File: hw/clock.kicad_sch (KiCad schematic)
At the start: 3 parts, among them SW1 SW_Push, U1 ATMEGA328PB-AU

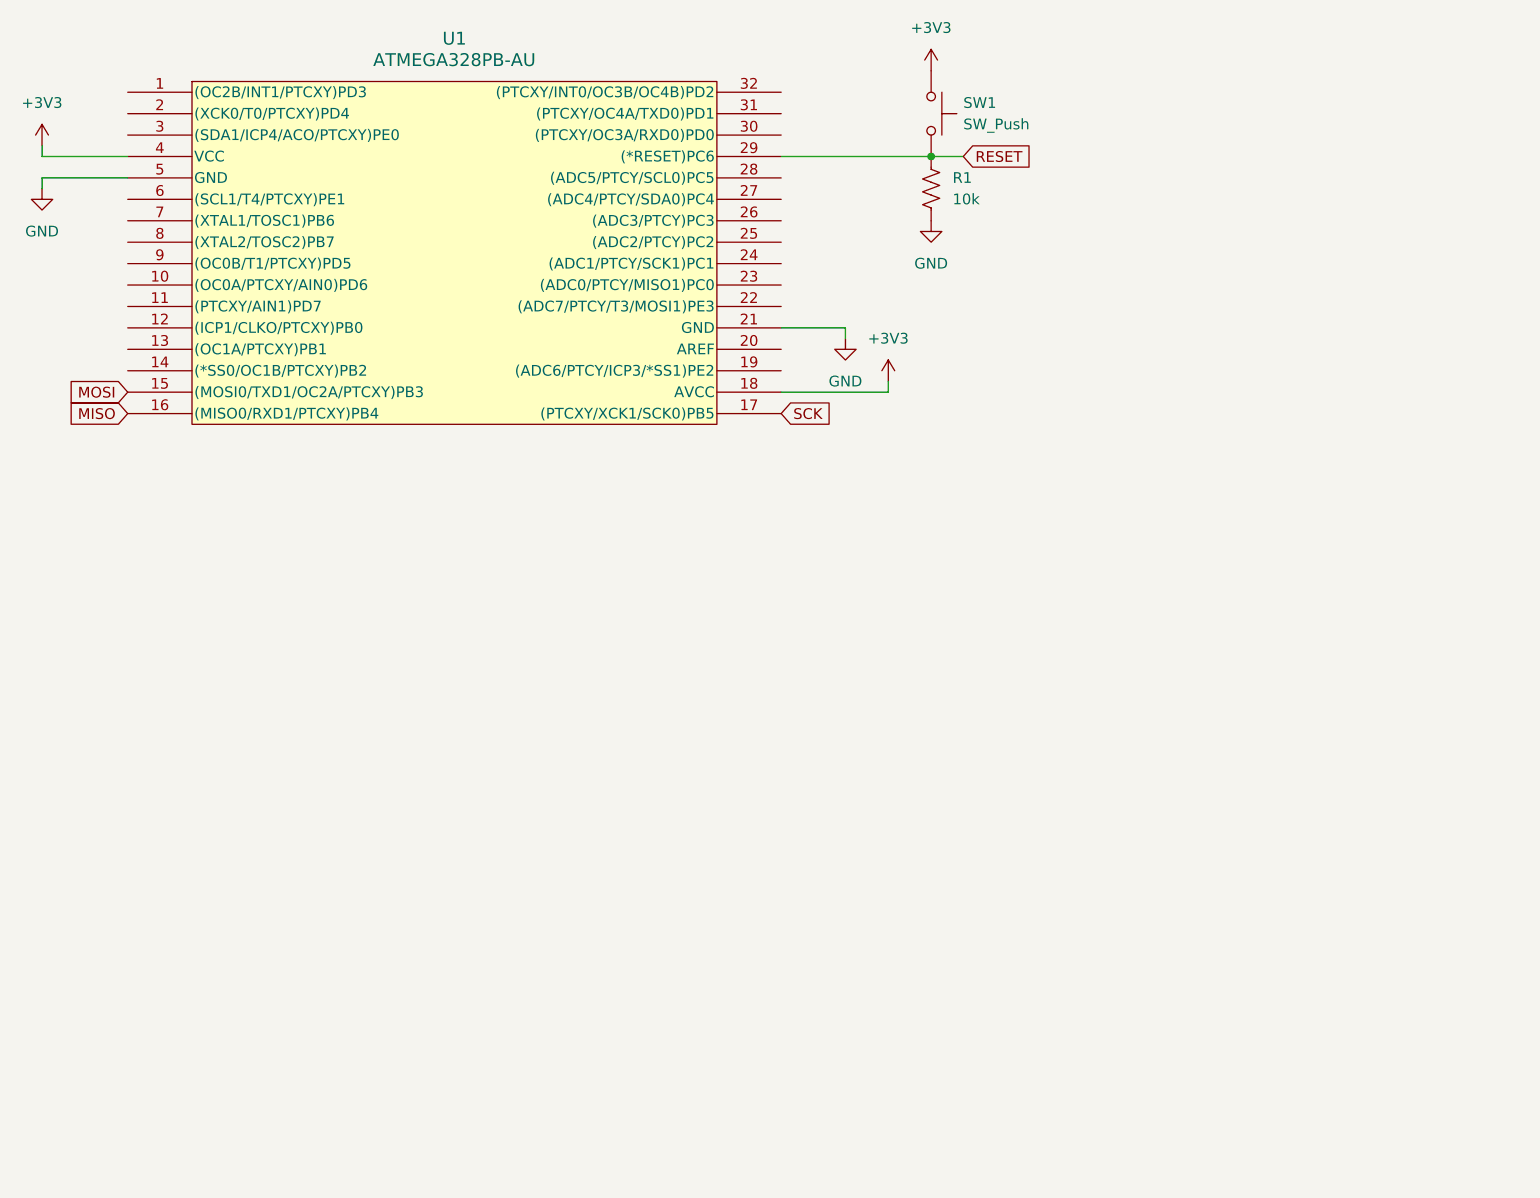
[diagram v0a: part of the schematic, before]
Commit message: Add USB
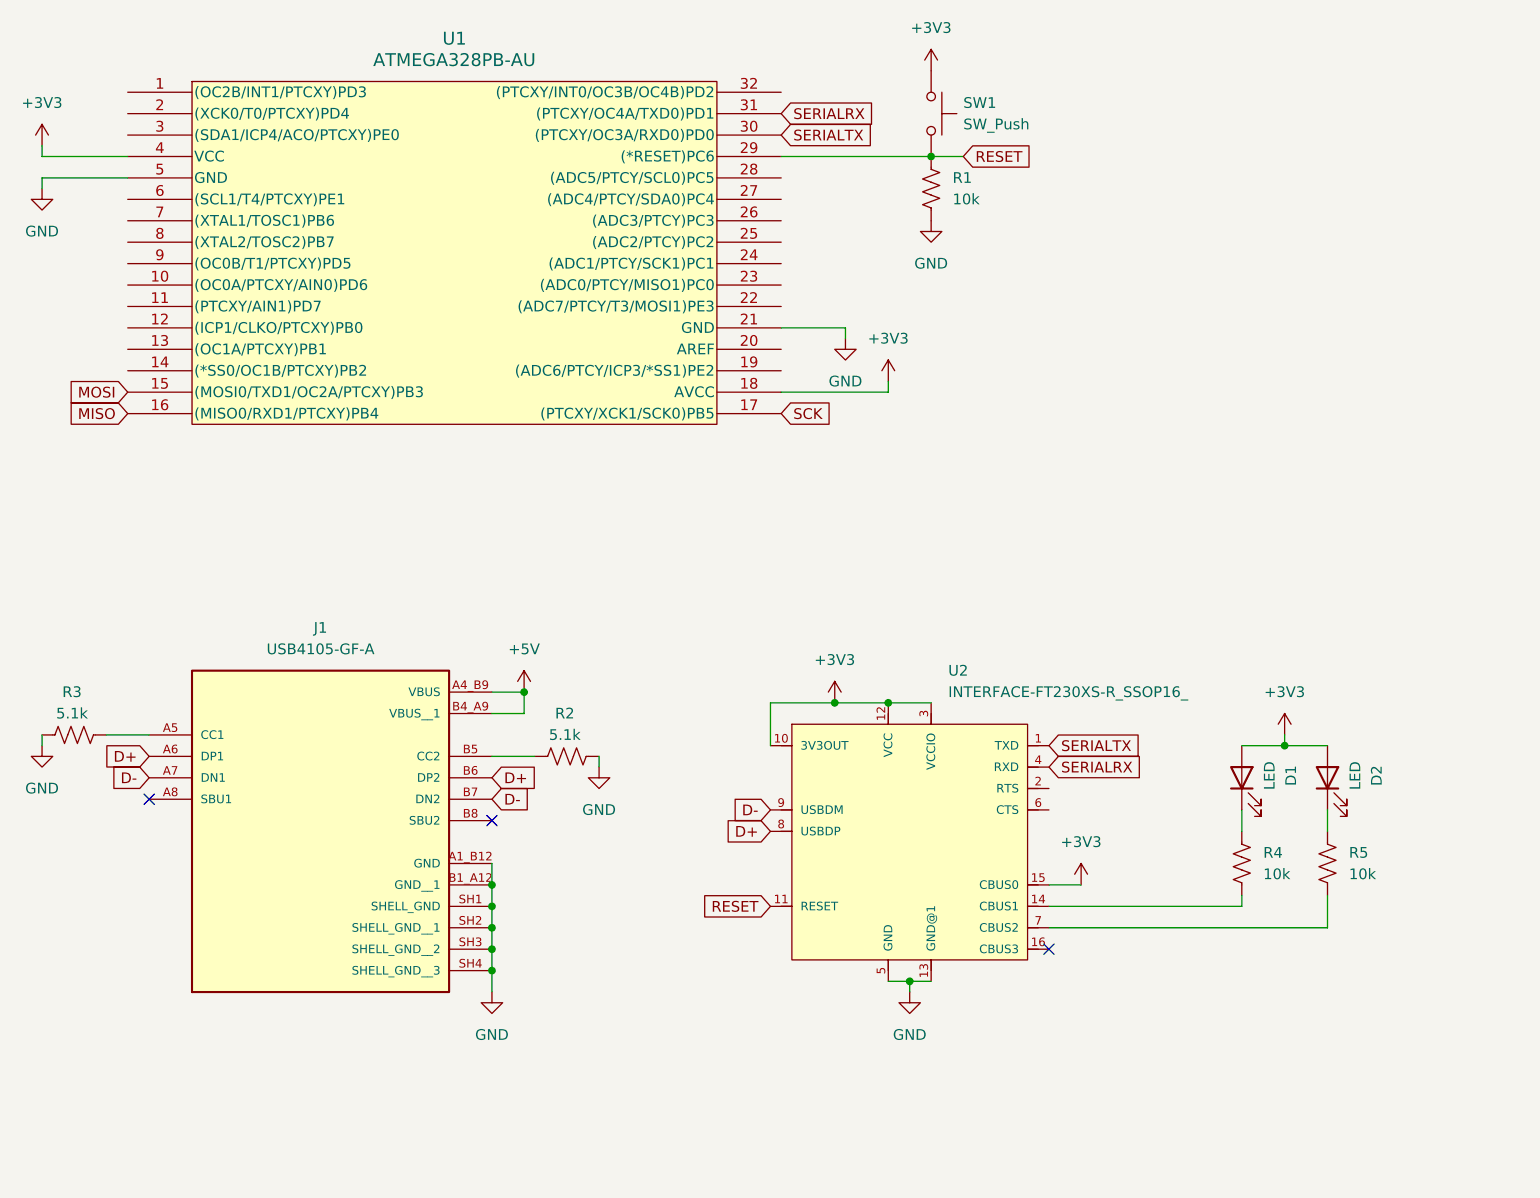
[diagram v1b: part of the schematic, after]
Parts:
- added D1, D2: LED, symbol Device:LED
- added J1: USB4105-GF-A, USB4105-GF-A:GCT_USB4105-GF-A, symbol USB4105-GF-A:USB4105-GF-A
- added R2, R3: 5.1k, symbol Device:R_US
- added R4, R5: 10k, symbol Device:R_US
- added U2: INTERFACE-FT230XS-R_SSOP16_, INTERFACE-FT230XS-R_SSOP16_:SSOP16-0.635-5X4MM, symbol INTERFACE-FT230XS-R_SSOP16_:INTERFACE-FT230XS-R_SSOP16_
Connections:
- net +3V3: now also D1.2 (A), D2.2 (A), U2.10 (3V3OUT), U2.12 (VCC), U2.15 (CBUS0), U2.3 (VCCIO)
- net GND: now also J1.A1_B12 (GND), J1.B1_A12 (GND__1), J1.SH1 (SHELL_GND), J1.SH2 (SHELL_GND__1), J1.SH3 (SHELL_GND__2), J1.SH4 (SHELL_GND__3), R2.1, R3.2, U2.13 (GND@1), U2.5 (GND)
- net RESET: now also U2.11 (RESET)
- net SERIALTX: now reaches U1.30 ((PTCXY/OC3A/RXD0)PD0)
- net SERIALTX: now also U2.1 (TXD)
- net SERIALRX: now reaches U1.31 ((PTCXY/OC4A/TXD0)PD1)
- net SERIALRX: now also U2.4 (RXD)
- new net: D1.1 (K), R4.2
- new net: D2.1 (K), R5.2
- new net: R4.1, U2.14 (CBUS1)
- new net: R5.1, U2.7 (CBUS2)
- new net: J1.A5 (CC1), R3.1
- new net: J1.B5 (CC2), R2.2
- new net +5V: J1.A4_B9 (VBUS), J1.B4_A9 (VBUS__1)
- new net D+: J1.A6 (DP1), J1.B6 (DP2), U2.8 (USBDP)
- new net D-: J1.A7 (DN1), J1.B7 (DN2), U2.9 (USBDM)
- no-connect marks 0 -> 3

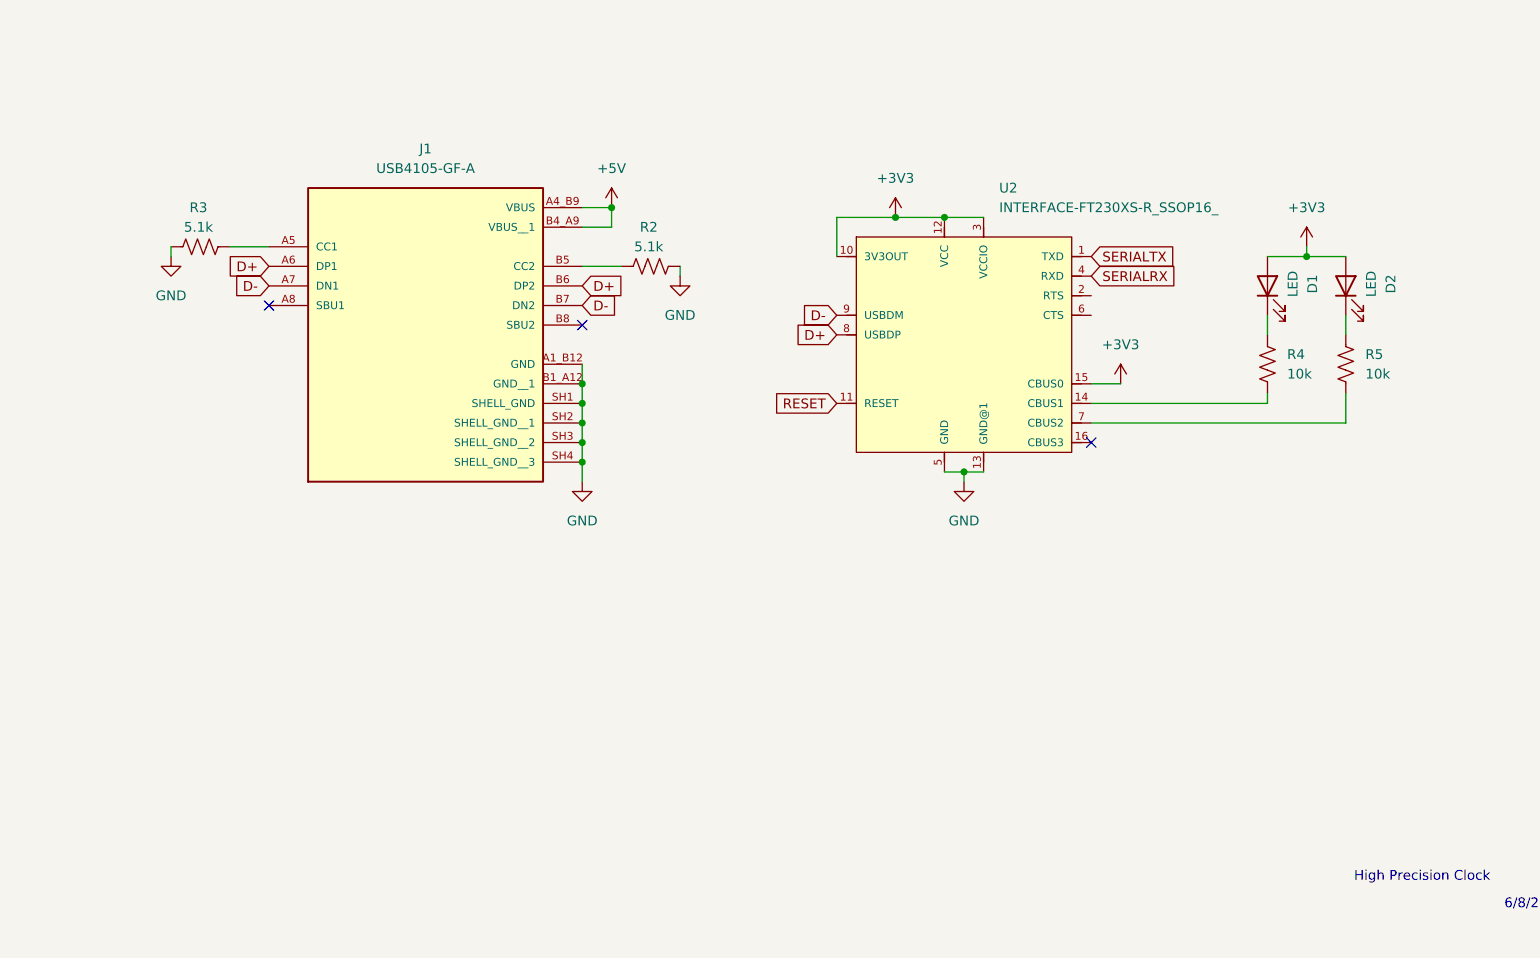
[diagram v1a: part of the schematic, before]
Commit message: Add voltage reg and serial converter
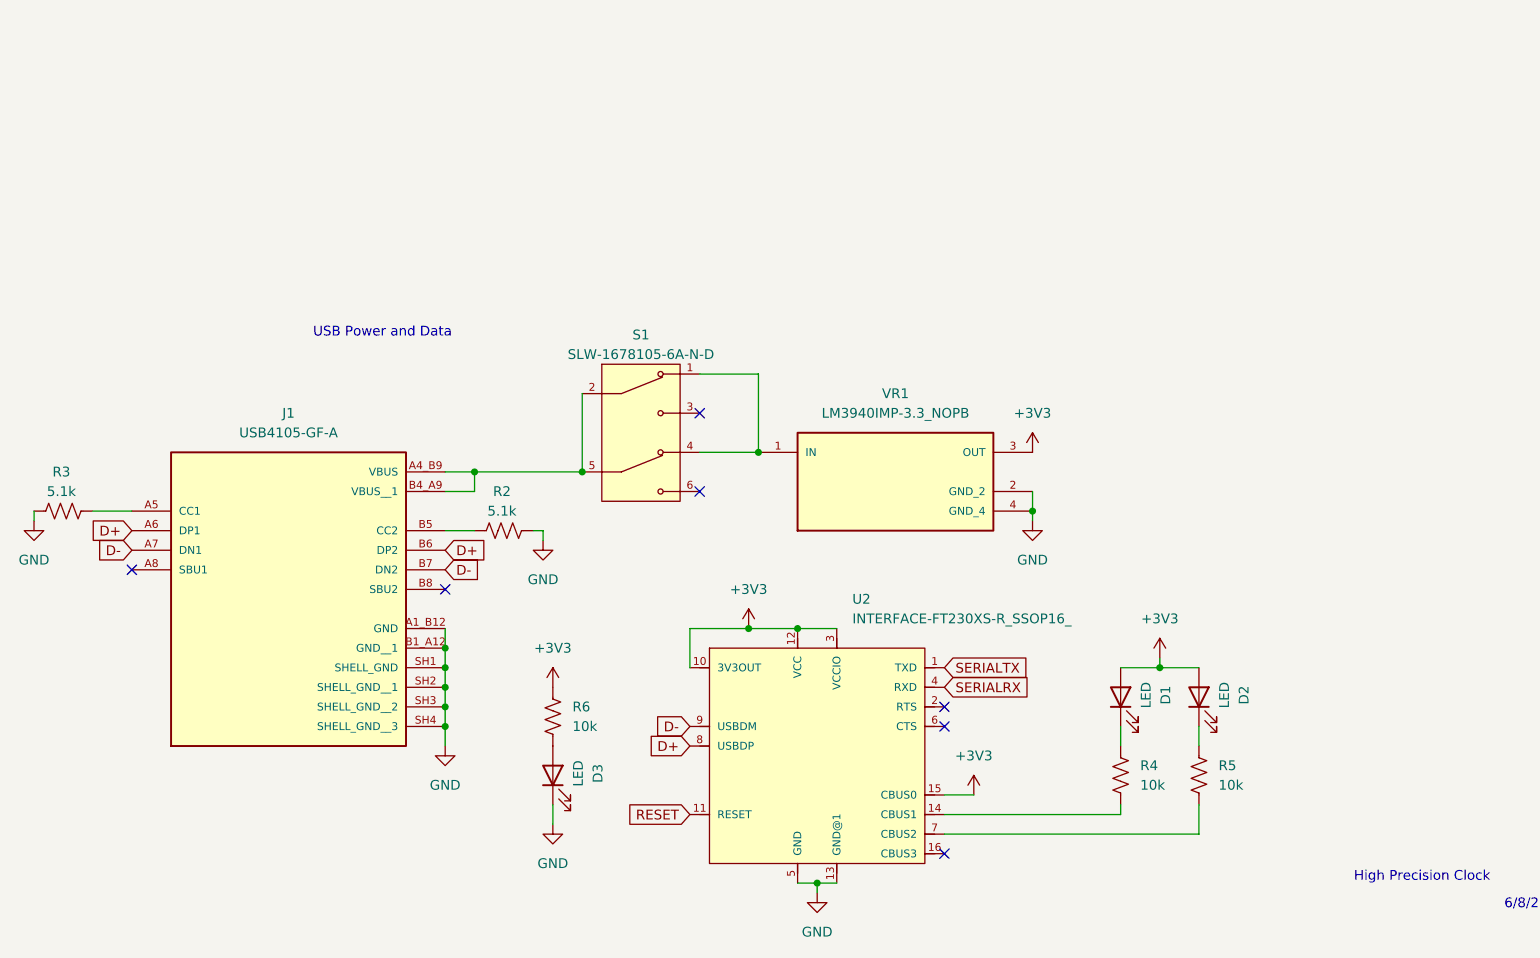
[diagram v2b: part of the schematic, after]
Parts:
- added D3: LED, LED_SMD:LED_0805_2012Metric, symbol Device:LED
- added R6: 10k, Resistor_SMD:R_0805_2012Metric, symbol Device:R_US
- added S1: SLW-1678105-6A-N-D, Clock:SW_SLW-1678105-6A-N-D, symbol SLW-1678105-6A-N-D:SLW-1678105-6A-N-D
- added VR1: LM3940IMP-3.3_NOPB, Clock:VREG_LM3940IMP-3.3_NOPB, symbol LM3940IMP-3.3_NOPB:LM3940IMP-3.3_NOPB
- D1, D2: footprint (none) -> LED_SMD:LED_0805_2012Metric
- J1: footprint USB4105-GF-A:GCT_USB4105-GF-A -> Clock:GCT_USB4105-GF-A
- R1, R2, R3, R4, R5: footprint (none) -> Resistor_SMD:R_0805_2012Metric
- U1: footprint 32A_MCH -> Clock:32A_MCH
- U2: footprint INTERFACE-FT230XS-R_SSOP16_:SSOP16-0.635-5X4MM -> Clock:SSOP16-0.635-5X4MM
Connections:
- net +3V3: now also R6.2, VR1.3 (OUT)
- net GND: now also D3.1 (K), VR1.2 (GND_2), VR1.4 (GND_4)
- net +5V: no longer names the net of J1.A4_B9 (VBUS), J1.B4_A9 (VBUS__1)
- net +5V: now also S1.2, S1.5
- new net: S1.1, S1.4, VR1.1 (IN)
- new net: D3.2 (A), R6.1
- no-connect marks 3 -> 7
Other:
- note added: "USB Power and Data"
- moved on the sheet: D1, D2, J1, R2, R3, R4, R5, U2

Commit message: Change mcu
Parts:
- removed R1: 10k, Resistor_SMD:R_0805_2012Metric, symbol Device:R_US
- removed SW1: SW_Push, symbol Switch:SW_Push
- removed U1: ATMEGA328PB-AU, Clock:32A_MCH, symbol 32A_MCH:ATMEGA328PB-AU
- added C1, C2: 20pf, symbol Device:C
- added R7: 10k, Resistor_SMD:R_0805_2012Metric, symbol Device:R_US
- added SW2: SW_Push, symbol Switch:SW_Push
- added U1: LPC812M101JDH20, Package_SO:TSSOP-20_4.4x6.5mm_P0.65mm, symbol MCU_NXP_LPC:LPC812M101JDH20
- added Y1: 30MHz, symbol Device:Crystal
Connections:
- net +3V3: now also SW2.1, U1.15 (VDD)
- net GND: now also C1.2, C2.1, R7.1, U1.16 (VSS)
- net RESET: now also R7.2, SW2.2, U1.4 (PIO0_5)
- net +5V: now reaches J1.A4_B9 (VBUS), J1.B4_A9 (VBUS__1), S1.2, S1.5
- net SERIALRX renamed SERIAL2
- net SERIAL2: now also U1.5 (PIO0_4)
- net SERIALTX renamed SERIAL1
- net SERIAL1: now also U1.19 (PIO0_0)
- new net: C1.1, U1.14 (PIO0_8), Y1.1
- new net: C2.2, U1.13 (PIO0_9), Y1.2
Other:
- note added: "RX"
- note added: "Serial lines used for audio data and programming"
- note added: "TX"

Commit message: Shift registers
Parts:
- removed SW2: SW_Push, symbol Switch:SW_Push
- added SW1: SW_Push, symbol Switch:SW_Push
- added U3, U4, U5, U6, U7, U8: SN74HC595DR, SN74HC595DR:SOIC127P600X175-16N, symbol SN74HC595DR:SN74HC595DR
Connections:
- net +3V3: now also U2.11 (RESET), SW1.1, U3.16 (VCC), U4.16 (VCC), U5.16 (VCC), U6.16 (VCC), U7.16 (VCC), U8.16 (VCC)
- net GND: now also U3.8 (GND), U4.8 (GND), U5.8 (GND), U6.8 (GND), U7.8 (GND), U8.8 (GND)
- net SHIFT_SER_0: now reaches U1.17 (PIO0_7)
- net SHIFT_SER_0: now also U3.14 (SER)
- net SHIFT_CLK: now reaches U1.18 (PIO0_6)
- net SHIFT_CLK: now also U3.11 (SRCLK), U4.11 (SRCLK), U5.11 (SRCLK), U6.11 (SRCLK), U7.11 (SRCLK), U8.11 (SRCLK)
- net SHIFT_SER_4: now reaches U1.2 (PIO0_13)
- net SHIFT_SER_4: now also U7.14 (SER)
- net SHIFT_SER_5: now reaches U1.20 (PIO0_14)
- net SHIFT_SER_5: now also U8.14 (SER)
- net SHIFT_SER_3: now reaches U1.3 (PIO0_12)
- net SHIFT_SER_3: now also U6.14 (SER)
- net SHIFT_RCLK: now reaches U1.6 (PIO0_3)
- net SHIFT_RCLK: now also U3.12 (RCLK), U4.12 (RCLK), U5.12 (RCLK), U6.12 (RCLK), U7.12 (RCLK), U8.12 (RCLK)
- net SHIFT_CLR: now reaches U1.7 (PIO0_2)
- net SHIFT_CLR: now also U3.10 (~{SRCLR}), U4.10 (~{SRCLR}), U5.10 (~{SRCLR}), U6.10 (~{SRCLR}), U7.10 (~{SRCLR}), U8.10 (~{SRCLR})
- net SHIFT_SER_2: now reaches U1.8 (PIO0_11)
- net SHIFT_SER_2: now also U5.14 (SER)
- net SHIFT_SER_1: now reaches U1.9 (PIO0_10)
- net SHIFT_SER_1: now also U4.14 (SER)
- net +5V: no longer names the net of J1.A4_B9 (VBUS), J1.B4_A9 (VBUS__1), S1.2, S1.5
- net RESET renamed SHIFT_OUT
- net SHIFT_OUT: now also SW1.2, U3.13 (~{OE}), U4.13 (~{OE}), U5.13 (~{OE}), U6.13 (~{OE}), U7.13 (~{OE}), U8.13 (~{OE}); no longer U2.11 (RESET)
- new net 0_A: U3.15 (QA)
- new net 0_B: U3.1 (QB)
- new net 0_C: U3.2 (QC)
- new net 0_D: U3.3 (QD)
- new net 0_E: U3.4 (QE)
- new net 0_F: U3.5 (QF)
- new net 0_G: U3.6 (QG)
- new net 0_H: U3.9 (QH)
- new net 1_A: U4.15 (QA)
- new net 1_B: U4.1 (QB)
- new net 1_C: U4.2 (QC)
- new net 1_D: U4.3 (QD)
- new net 1_E: U4.4 (QE)
- new net 1_F: U4.5 (QF)
- new net 1_G: U4.6 (QG)
- new net 1_H: U4.9 (QH)
- new net 2_A: U5.15 (QA)
- new net 2_B: U5.1 (QB)
- new net 2_C: U5.2 (QC)
- new net 2_D: U5.3 (QD)
- new net 2_E: U5.4 (QE)
- new net 2_F: U5.5 (QF)
- new net 2_G: U5.6 (QG)
- new net 2_H: U5.9 (QH)
- new net 3_A: U6.15 (QA)
- new net 3_B: U6.1 (QB)
- new net 3_C: U6.2 (QC)
- new net 3_D: U6.3 (QD)
- new net 3_E: U6.4 (QE)
- new net 3_F: U6.5 (QF)
- new net 3_G: U6.6 (QG)
- new net 3_H: U6.9 (QH)
- new net 4_A: U7.15 (QA)
- new net 4_B: U7.1 (QB)
- new net 4_C: U7.2 (QC)
- new net 4_D: U7.3 (QD)
- new net 4_E: U7.4 (QE)
- new net 4_F: U7.5 (QF)
- new net 4_G: U7.6 (QG)
- new net 4_H: U7.9 (QH)
- new net 5_A: U8.15 (QA)
- new net 5_B: U8.1 (QB)
- new net 5_C: U8.2 (QC)
- new net 5_D: U8.3 (QD)
- new net 5_E: U8.4 (QE)
- new net 5_F: U8.5 (QF)
- new net 5_G: U8.6 (QG)
- new net 5_H: U8.9 (QH)
- no-connect marks 7 -> 13
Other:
- note added: "Reset"
- moved on the sheet: C1, C2, R7, U1, Y1

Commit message: RTC
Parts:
- added C3, C4: ~, symbol Device:C
- added R1, R10, R8, R9: 10k, Resistor_SMD:R_0805_2012Metric, symbol Device:R_US
- added SW2: SW_Push, symbol Switch:SW_Push
- added U9: MCP7940MT-I_SN, MCP7940MT-I_SN:SOIC127P600X175-8N, symbol MCP7940MT-I_SN:MCP7940MT-I_SN
- added Y2: 32.768KHz, symbol Device:Crystal
- C1, C2: value 20pf -> ~
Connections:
- net +3V3: now also R7.2, R8.2, R9.2, SW2.1, U9.8 (VCC)
- net GND: now also C3.2, C4.1, R1.1, R10.1, U9.4 (VSS); no longer R7.1
- net SHIFT_CLR: now also U1.3 (PIO0_12), R10.2, SW2.2; no longer U1.7 (PIO0_2)
- net SHIFT_OUT: now also R1.2; no longer R7.2
- net SHIFT_SER_1: now also U1.2 (PIO0_13); no longer U1.9 (PIO0_10)
- net SHIFT_SER_2: now also U1.20 (PIO0_14); no longer U1.8 (PIO0_11)
- net SHIFT_SER_3: now also U1.11 (PIO0_15); no longer U1.3 (PIO0_12)
- net SHIFT_SER_4: now also U1.10 (PIO0_16); no longer U1.2 (PIO0_13)
- net SHIFT_SER_5: now also U1.1 (PIO0_17); no longer U1.20 (PIO0_14)
- net GPS_PPS: now reaches U1.12 (PIO0_1)
- new net: C3.1, U9.1 (X1), Y2.1
- new net: C4.2, U9.2 (X2), Y2.2
- new net RTC_PPS: R9.1, U1.7 (PIO0_2), U9.7 (MFP)
- new net SCL: R7.1, U1.9 (PIO0_10), U9.6 (SCL)
- new net SDA: R8.1, U1.8 (PIO0_11), U9.5 (SDA)
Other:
- note added: "Control and Clock Gen"
- note added: "ISP Mode"
- note added: "Shift Registers"
- moved on the sheet: C1, C2, D1, D2, D3, J1, R2, R3, R4, R5, R6, S1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
